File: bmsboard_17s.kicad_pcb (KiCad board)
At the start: 2 copper layers, 100 x 90 mm, 253 parts, among them J2 Conn_01x08, J3 Conn_01x02, J4 Conn_01x04, J5 Conn_01x02, J6 Conn_01x02, Q1 Q_NMOS_GDS, Q10 Q_NMOS_GDS, Q11 Q_NMOS_GDS, Q12 Q_NMOS_GDS, Q13 Q_NMOS_GDS, Q14 Q_NMOS_GDS, Q15 Q_NMOS_GDS, Q16 Q_NMOS_GDS, Q17 Q_NMOS_GDS, Q18 Q_NMOS_GDS, Q19 Q_NMOS_GDS, Q2 Q_NMOS_GDS, Q20 Q_NMOS_GDS, Q21 Q_NMOS_GDS, Q22 Q_NMOS_GDS, Q23 Q_NMOS_GDS, Q24 Q_NMOS_GDS, Q25 Q_NMOS_GDS, Q26 Q_NMOS_GDS, Q27 PMOS, Q28 PMOS, Q29 Q_NMOS_GDS, Q3 Q_PMOS_GDS, Q30 Q_NMOS_GDS, Q31 Q_NMOS_GDS, Q32 Q_NMOS_GDS, Q33 Q_NMOS_GDS, Q34 Q_NMOS_GDS, Q35 Q_NMOS_GDS, Q36 Q_NMOS_GDS, Q37 Q_NMOS_GDS, Q38 Q_NMOS_GDS, Q4 Q_NPN_BEC, Q5 Q_NPN_BEC, Q6 Q_NPN_BEC, Q7 Q_NPN_BEC, Q8 Q_NPN_BEC, Q9 Q_NPN_BEC, U1 PB7170, U10 TJA1042T-3, U11 MAX485E, U12 PY32F003F1xUx, U2 CH32V103C8T6, U3 XTSD01G, U4 74HC138, U5 BMP280, U7 Si7020-A20, U8 QMA6100P, U9 ADS1243, Y1 16MHz, Y2 32.768kHz

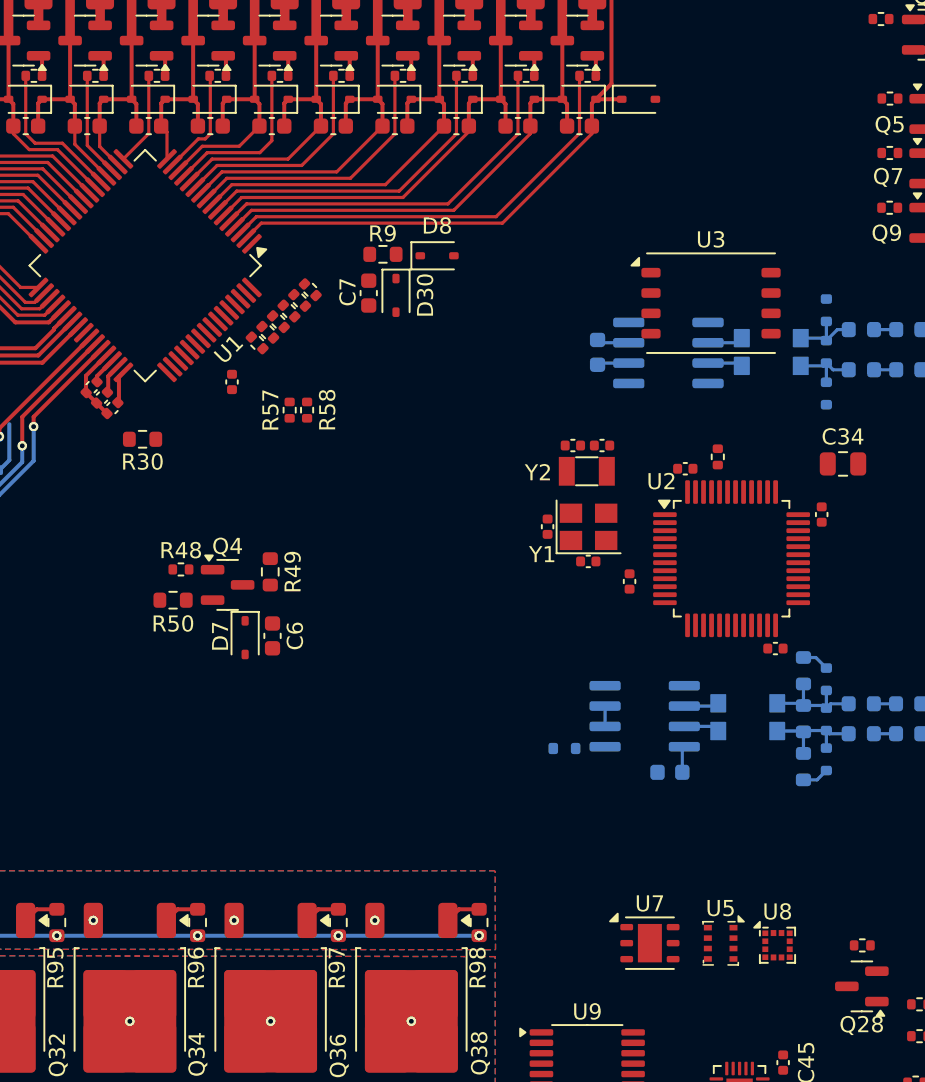
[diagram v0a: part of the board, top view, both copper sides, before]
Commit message: 修改电源电路
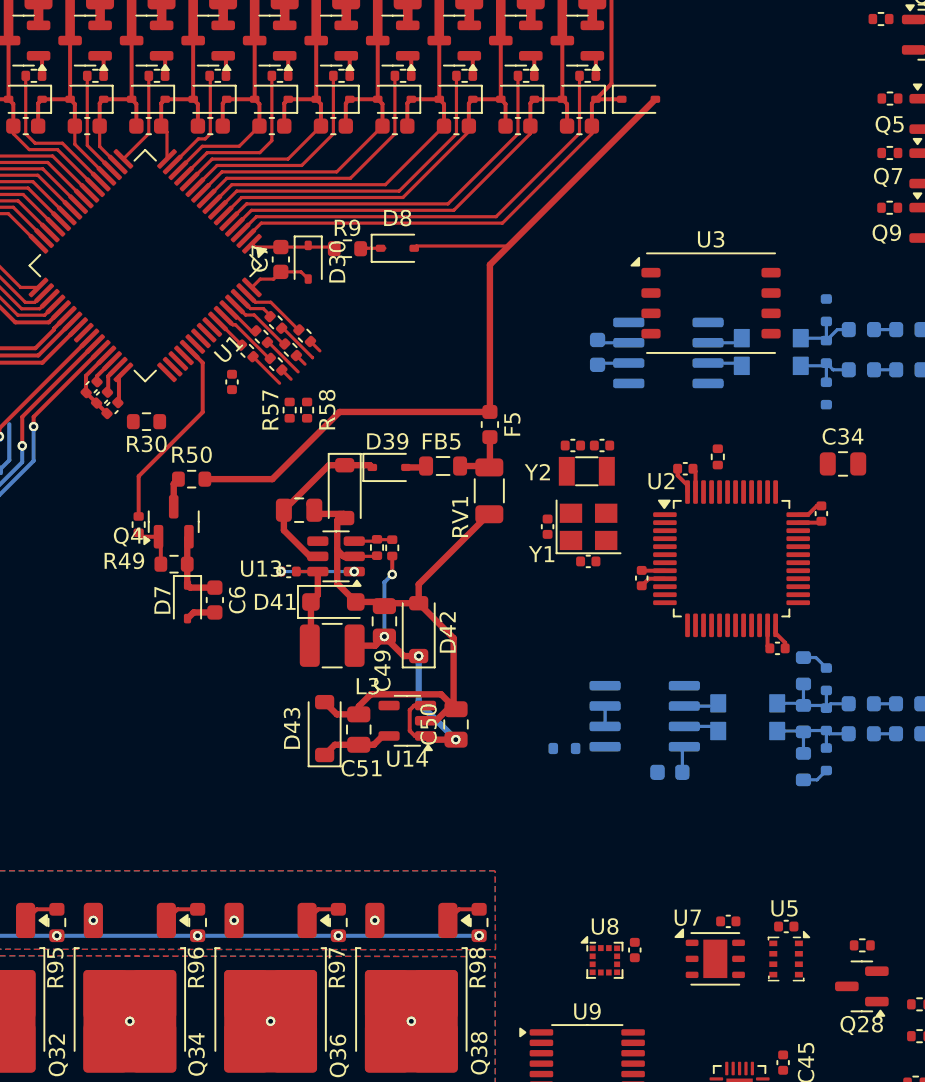
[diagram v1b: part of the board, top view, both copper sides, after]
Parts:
- added C47: 100nF, Capacitor_SMD:C_0402_1005Metric, F.Cu at (73.0, 71.2)
- added C48: 1uF 100V, Capacitor_SMD:C_0805_2012Metric, F.Cu at (73.7, 67.3)
- added C49: 10uF, Capacitor_SMD:C_0805_2012Metric, F.Cu at (79.0, 74.3)
- added C50: 10uF, Capacitor_SMD:C_0805_2012Metric, F.Cu at (83.5, 80.7)
- added C51: 10uF, Capacitor_SMD:C_0805_2012Metric, F.Cu at (77.4, 81.0)
- added C52: 0.1uF, Capacitor_SMD:C_0402_1005Metric, F.Cu at (104.1, 93.3)
- added C53: 0.1uF, Capacitor_SMD:C_0402_1005Metric, F.Cu at (100.5, 93.0)
- added C54: 0.1uF, Capacitor_SMD:C_0402_1005Metric, F.Cu at (94.6, 94.8)
- added D39: D, Diode_SMD:D_SOD-323, F.Cu at (79.3, 64.7)
- added D40: D_Zener, Diode_SMD:D_SOD-123, F.Cu at (76.5, 66.2)
- added D41: DSK210, Diode_SMD:D_SOD-123F, F.Cu at (75.8, 73.1)
- added D42: D_Zener, Diode_SMD:D_SOD-123, F.Cu at (81.1, 74.8)
- added D43: D_Zener, Diode_SMD:D_SOD-123, F.Cu at (75.3, 81.0)
- added F5: 100mA, Fuse:Fuse_0603_1608Metric, F.Cu at (85.6, 62.0)
- added FB5: 120, Inductor_SMD:L_0805_2012Metric, F.Cu at (82.7, 64.6)
- added L3: 47uH, Inductor_SMD:L_1210_3225Metric, F.Cu at (75.7, 75.8)
- added R100: 240k, Resistor_SMD:R_0402_1005Metric, F.Cu at (79.5, 69.7)
- added R99: 10k, Resistor_SMD:R_0402_1005Metric, F.Cu at (78.5, 69.7)
- added RV1: Varistor, Resistor_SMD:R_1206_3216Metric, F.Cu at (85.5, 66.1)
- added U13: YX59012, Package_TO_SOT_SMD:SOT-23-6, F.Cu at (76.0, 70.2)
- added U14: SGM2033-3.3, Package_TO_SOT_SMD:SOT-23-5, F.Cu at (80.4, 80.5)
- R51, R52, R53, R54, R55, R56: value 1k -> 100
- moved U8 10.8 mm to (92.8, 95.4)
- moved R50 7.65 mm to (67.0, 65.4), turned to 180 degrees
- moved R49 6.03 mm to (65.8, 70.7), turned to 0 degrees
- moved C7 5.88 mm to (72.5, 51.7)
- moved D30 5.86 mm to (74.2, 51.8)
- moved Q4 5.19 mm to (65.8, 68.0), turned to 90 degrees
- moved D7 4.24 mm to (66.7, 73.0)
- moved C6 4.24 mm to (68.4, 72.9)
- moved U5 4.20 mm to (104.1, 95.4)
- moved U7 4.20 mm to (99.7, 95.3)
- moved R48 3.85 mm to (63.6, 68.2), turned to -90 degrees
- moved R56 2.89 mm to (74.0, 56.4)
- moved D8 2.52 mm to (79.8, 51.0)
- moved R54 2.42 mm to (73.1, 57.3)
- moved R9 2.24 mm to (76.7, 51.0)
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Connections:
- net /AFE Module/BAT+ renamed BAT+
- C34 pad 1: VDD -> +3.3V
- C35 pad 1: VDD -> +3.3V
- C37 pad 1: VDD -> +3.3V
- C38 pad 1: VDD -> +3.3V
- C39 pad 1: VDD -> +3.3V
- U2 pad 1: VDD -> +3.3V
- U2 pad 19: /MCU Module/WDET_PWM -> unconnected-(U2-PB1-Pad19)
- U2 pad 20: /MCU Module/WDET_EN -> unconnected-(U2-PB2-Pad20)
- U2 pad 24: VDD -> +3.3V
- U2 pad 36: VDD -> +3.3V
- U2 pad 48: VDD -> +3.3V
- U2 pad 9: VDD -> +3.3V
- U8 pad 10: unconnected-(U8-~{CS}-Pad10) -> +3.3V
- U8 pad 12: unconnected-(U8-SCx-Pad12) -> /Sensors Module/SCL
- U8 pad 2: unconnected-(U8-SDx-Pad2) -> /Sensors Module/SDA
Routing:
- net BAT+: track 0.00 -> 62.3 mm
- net GND: track 55.6 -> 108.6 mm
- net Net-(D42-K): track 0.00 -> 21.7 mm, vias 0 -> 4
- net +3.3V: track 0.00 -> 16.1 mm
- net /AFE Module/DRIVE: track 0.00 -> 12.4 mm
- net Net-(D39-K): track 0.00 -> 10.8 mm
- net Net-(D41-K): track 0.00 -> 6.18 mm
- net Net-(D30-K): track 0.00 -> 5.57 mm
- net Net-(U13-CB): track 0.00 -> 4.61 mm, vias 0 -> 2
- net Net-(U1-SCLK): track 0.00 -> 4.25 mm
- net Net-(U1-SDI): track 0.00 -> 4.14 mm
- net Net-(U1-GPIO2): track 0.00 -> 4.02 mm
- net Net-(F5-Pad2): track 0.00 -> 3.77 mm
- net Net-(Q4-B): track 0.00 -> 3.12 mm
- net /CS_AFE: track 0.00 -> 2.70 mm
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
